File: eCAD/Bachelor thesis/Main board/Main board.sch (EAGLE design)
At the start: 114 parts, among them IC1 ESP32-WROOM-32E_M113EH3200PH3Q, IC10 SMS3.3.TCT, IC2 BC660K-GL, IC3 SMS3.3.TCT, IC4 AP9101CK6-ADTRG1, IC5 FDS6898A, IC6 MCP73871-2CCI_ML, IC7 ME6211C33M5G-N, IC8 ME6211C33M5G-N, IC9 SMS3.3.TCT, J1 U.FL-R-SMT(10), J2 SIM7100-6-1-15-00-A, J3 XT30PW-M, J4 RJE01-660-01, J5 RJE01-660-01, J6 RJE01-660-01, Q1 PDTC114EU,115, Q2 PDTC114EU,115, Q3 IRF7319TRPBF, Q4 IRF7319TRPBF

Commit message: Main board .brd added
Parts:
- removed R35, R36: 10k, rcl:R-EU_R0805
- removed S1, S2, S3, S4, S5: TS-1088-AR02016, 1-component-search:TS-1088-AR02016
- removed TP1, TP2: TPB2,54, testpad:TPB2,54
- added C29: 100n, rcl:C-EUC0805
- added JP10: FAN, jumper:JP2E
- added JP11: LED_VDD, jumper:JP1E
- added JP6: ESP_UART, jumper:JP4E
- added JP8: NB_UART_DEBUG, jumper:JP1E
- added JP9: NTC, jumper:JP1E
- C1: value 470u -> 1u; device rcl:CPOL-EUD -> rcl:C-EUC0805
- C11: value 33p -> 22p
- C13: value 33p -> 100n
- C14: value 100n -> 470u; device rcl:C-EUC0805 -> rcl:CPOL-EUD
- C15: value 100n -> (none)
- C17: value 10u -> 100n
- C18: value 4u7 -> 100n
- C19: value 1u -> 10u
- C2: value 1u -> 470u; device rcl:C-EUC0805 -> rcl:CPOL-EUD
- C20, C23: value 1u -> 4u7
- C21: value 4u7 -> 1u
- C24: value 100n -> 1u
- C25: value 50 -> 1u; device rcl:CPOL-EUE5-10.5 -> rcl:C-EUC0805
- C26: value 22u -> 50; device rcl:C-EUC0805 -> rcl:CPOL-EUE5-10.5
- C4: value 470u -> 22u; device rcl:CPOL-EUD -> rcl:C-EUC0805
- C6: value 22p -> 33p
- C7: value 100p -> 33p
- C9: value (none) -> 100p
- JP1: device pinhead:PINHD-1X3 -> jumper:JP1E
- JP2: value ESP_UART -> (none); device jumper:JP4E -> jumper:JP1E
- JP3: value NB_UART -> (none); device jumper:JP4E -> jumper:JP1E
- JP4: value NTC -> (none)
- JP5: value LED_VDD -> (none)
- JP7: value FAN -> NB_UART; device jumper:JP2E -> jumper:JP4E
- LED1: value STAT1 -> NETSTAT
- R10: value (none) -> 2k7
- R11: value 2k2 -> 1M; device rcl:R-EU_R1206 -> rcl:R-EU_R0805
- R12: value 2k7 -> 5k1
- R13: value 1M -> 5k1
- R14: value 5k1 -> 330R
- R15: value 5k1 -> (none)
- R16: value 330R -> (none)
- R17, R18: value (none) -> 470
- R20, R21: value 470 -> 10k
- R23: value 10k -> 1k
- R24: value 10k -> (none)
- R25: value 1k -> (none)
- R26, R27: value (none) -> 4k7
- R29: value 10k -> 4k7
- R30, R31, R32: value 4k7 -> 10k
- R4: value 10K -> 10k
- R5: value 10K -> 22
- R6: value 10k -> 22
- R8: value 22 -> (none)
- R9: value 22 -> 2k2; device rcl:R-EU_R0805 -> rcl:R-EU_R1206
- renumbered $3_24_$_2023-03-17_12-09-30 to $3_29_$_2023-03-21_17-43-41, $3_25_$_2023-03-17_12-09-30 to $3_30_$_2023-03-21_17-43-41
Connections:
- removed net BAT+: Q3.S2, R33.1
- removed net BOOT_N: IC1.IO19, R4.2, S4.NO
- removed net ESP_PIN: IC1.IO33, Q3.G1, Q4.G1, R28.2, R29.2
- removed net PSM_EINT_N: IC1.IO5, R5.2, S5.NO
- removed net RESET_EN: IC1.IO18, R3.2, S3.NO
- new net DRIVE_PIN: IC1.IO33, Q3.G1, Q4.G1, R28.2, R30.2
- net !PG: now also R17.2, R20.2; no longer R19.2, R22.2
- net !TE1: now also R23.1; no longer R25.1
- net BAT-: now also C18.2; no longer C16.2
- net BAT_Q: now also R20.1, R21.1, R33.2; no longer R23.1, R24.1, R35.2
- net BOOT: now also JP4.1
- net CC3: now also R13.1; no longer R15.1
- net CC4: now also R12.1; no longer R14.1
- net DS18B_SIG: now also R29.1; no longer R32.1
- net ESP_EN: now also C1.1, JP1.2; no longer C2.1, JP1.3, S1.NO
- net ESP_FLASH: now also JP2.2; no longer S2.COM
- net FLASH_RX: now also JP6.3; no longer JP2.3
- net FLASH_TX: now also JP6.2; no longer JP2.2
- net GND: now also C1.2, C14.-, C2.-, C25.2, C26.-, C29.2, C3.2, C4.1, C5.1, JP10.1, JP2.1, JP3.2, JP4.2, JP6.4, JP7.4, JP9.1, R10.1, R11.2, R12.2, R16.2, R23.2, R24.2, R30.1, R34.1; no longer C1.-, C18.2, C2.2, C25.-, C26.1, C3.1, C4.-, C5.2, JP1.2, JP2.4, JP3.4, JP4.1, JP7.1, R12.1, R14.2, R15.2, R18.2, R26.2, R27.2, R29.1, R36.1, R4.1, R5.1, S1.COM, S2.NO
- net G_BAT: now also R31.2; no longer R33.2
- net G_SENS: now also R32.2; no longer R34.2
- net I2C_SCL: now also R27.1; no longer R31.1
- net I2C_SDA: now also R26.1; no longer R30.1
- net N$1: now also JP8.1; no longer TP1.TP
- net N$16: now also R9.2; no longer R11.2
- net N$17: now also R9.1; no longer R11.1
- net N$19: now also C12.1, R8.1; no longer C9.1, R10.1
- net N$2: now also JP8.2; no longer TP2.TP
- net N$20: now also C15.1, R8.2; no longer C12.1, R10.2
- net N$21: now also C7.1, R5.2; no longer C10.1, R7.2
- net N$22: now also C8.1, R6.2; no longer C11.1, R8.2
- net N$23: now also C10.1, R7.2; no longer C13.1, R9.2
- net N$5: now also C18.1, R14.1; no longer C16.1, R16.1
- net N$6: now also IC8.CE, JP10.2; no longer IC7.CE, JP7.2
- net N$7: now also R17.1; no longer R19.1
- net N$8: now also R18.1; no longer R20.1
- net N$9: now also R19.1; no longer R21.1
- net OUT: now also C20.1; no longer C18.1
- net PROG2: now also R24.1; no longer R26.1
- net PROG4: now also R25.1; no longer R27.1
- net PSM_EINT: now also IC1.IO5, JP5.1, R3.2
- net RESET_N: now also C17.1, C3.1, JP3.1; no longer C15.1
- net RESET_QUECTEL: now also IC1.IO18
- net S1: now also R11.1; no longer R13.1
- net SENS_VDD33: now also R26.2, R27.2, R29.2; no longer R30.2, R31.2, R32.2
- net STAT1: now also R19.2, R22.2; no longer R21.2, R24.2
- net STAT2: now also R18.2, R21.2; no longer R20.2, R23.2
- net THERM1: now also JP9.2; no longer JP4.2
- net UART_MCU_RX: now also JP7.2; no longer JP3.2
- net UART_MCU_TX: now also JP7.3; no longer JP3.3
- net USIM_CLK: now also R6.1; no longer R8.1
- net USIM_DATA: now also R4.2, R7.1; no longer R6.2, R9.1
- net USIM_GND: now also C16.2; no longer C14.2
- net USIM_RST: now also R5.1; no longer R7.1
- net USIM_VDD: now also C16.1, C6.1, R4.1; no longer C14.1, C8.1, R6.1
- net VBAT: now also C23.1, Q3.S2, R14.2, R31.1; no longer C21.1, R16.2
- net VDD33: now also C11.1, C13.1, C14.+, C2.+, C24.1, C26.+, C4.2, C5.2, C9.1, IC7.VOUT, JP11.2, JP6.1, JP7.1, R32.1; no longer C1.+, C23.1, C25.+, C26.2, C3.2, C4.+, C5.1, C6.1, C7.1, IC8.VOUT, JP2.1, JP3.1, R34.1, S3.COM, S4.COM, S5.COM
- net VDD_FAN: now also C25.1, IC8.VOUT; no longer C22.1, IC7.VOUT
- net VDD_LED: now also JP11.1; no longer JP5.1
- net VIN: now also C21.1, IC8.VIN, JP10.3, R15.2; no longer C17.1, IC7.VIN, JP7.3, R17.2
- net VIN_LDO: now also C22.1, IC7.CE, IC7.VIN; no longer C20.1, IC8.CE, IC8.VIN
- net VM1: now also R10.2; no longer R12.2
- net VOL_SENS: now also C29.1, R33.1, R34.2; no longer C24.1, R35.1, R36.2
- net VPCC1: now also R15.1, R16.1; no longer R17.1, R18.1
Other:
- moved on the sheet: C10, C11, C12, C13, C15, C18, C19, C20, C21, C22, C23, C3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

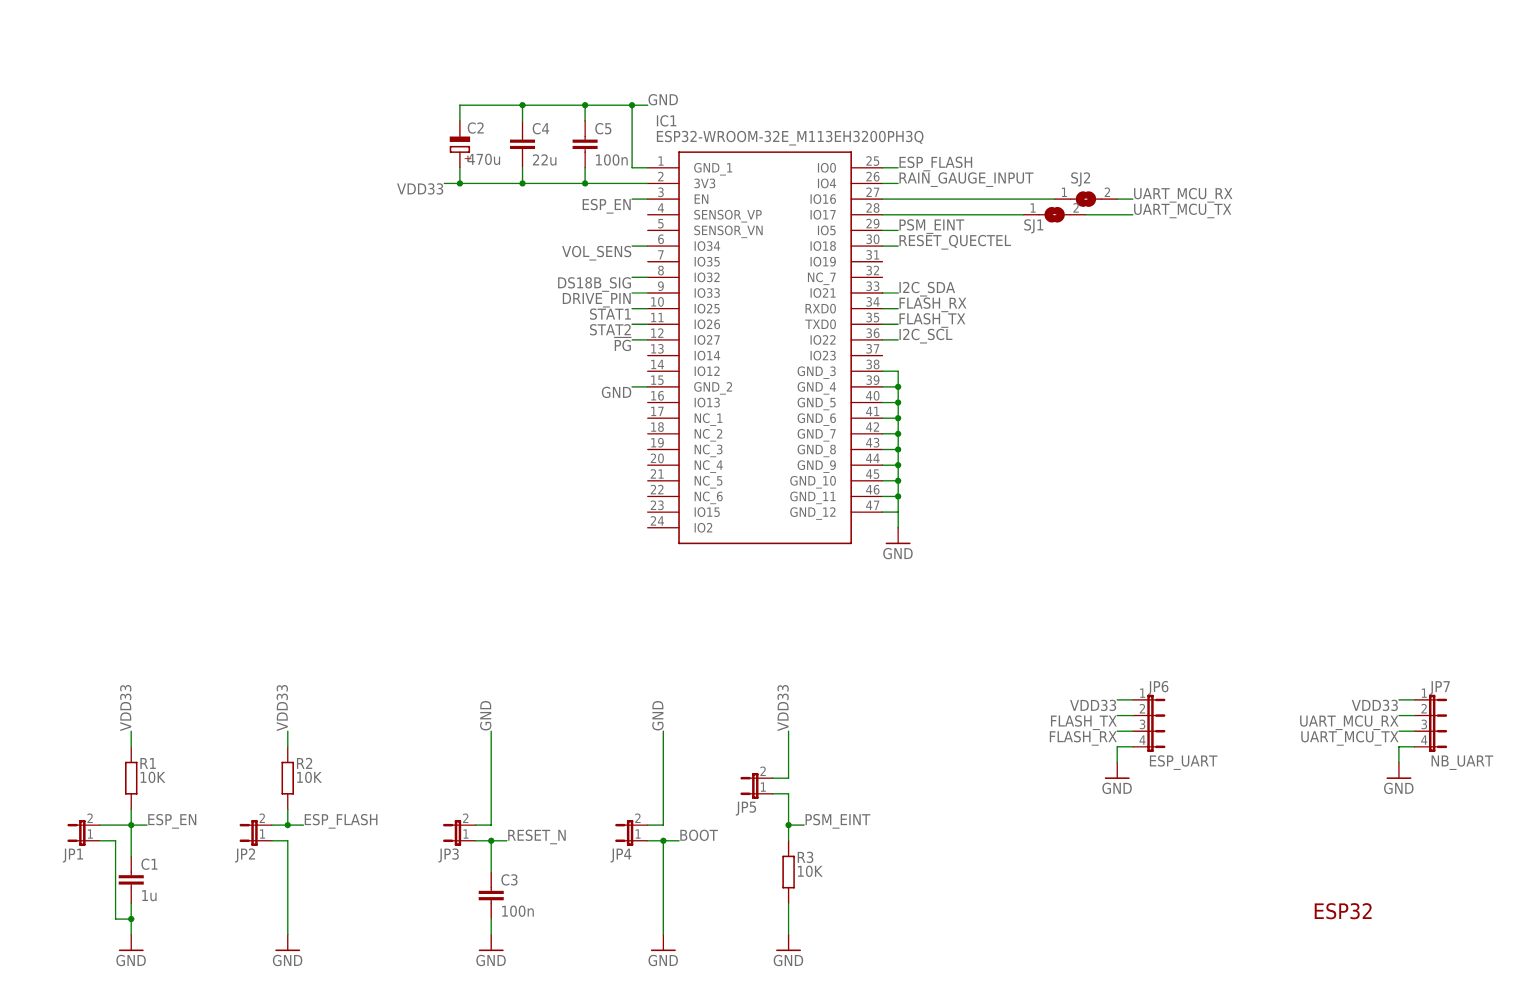
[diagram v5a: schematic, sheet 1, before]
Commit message: component placement
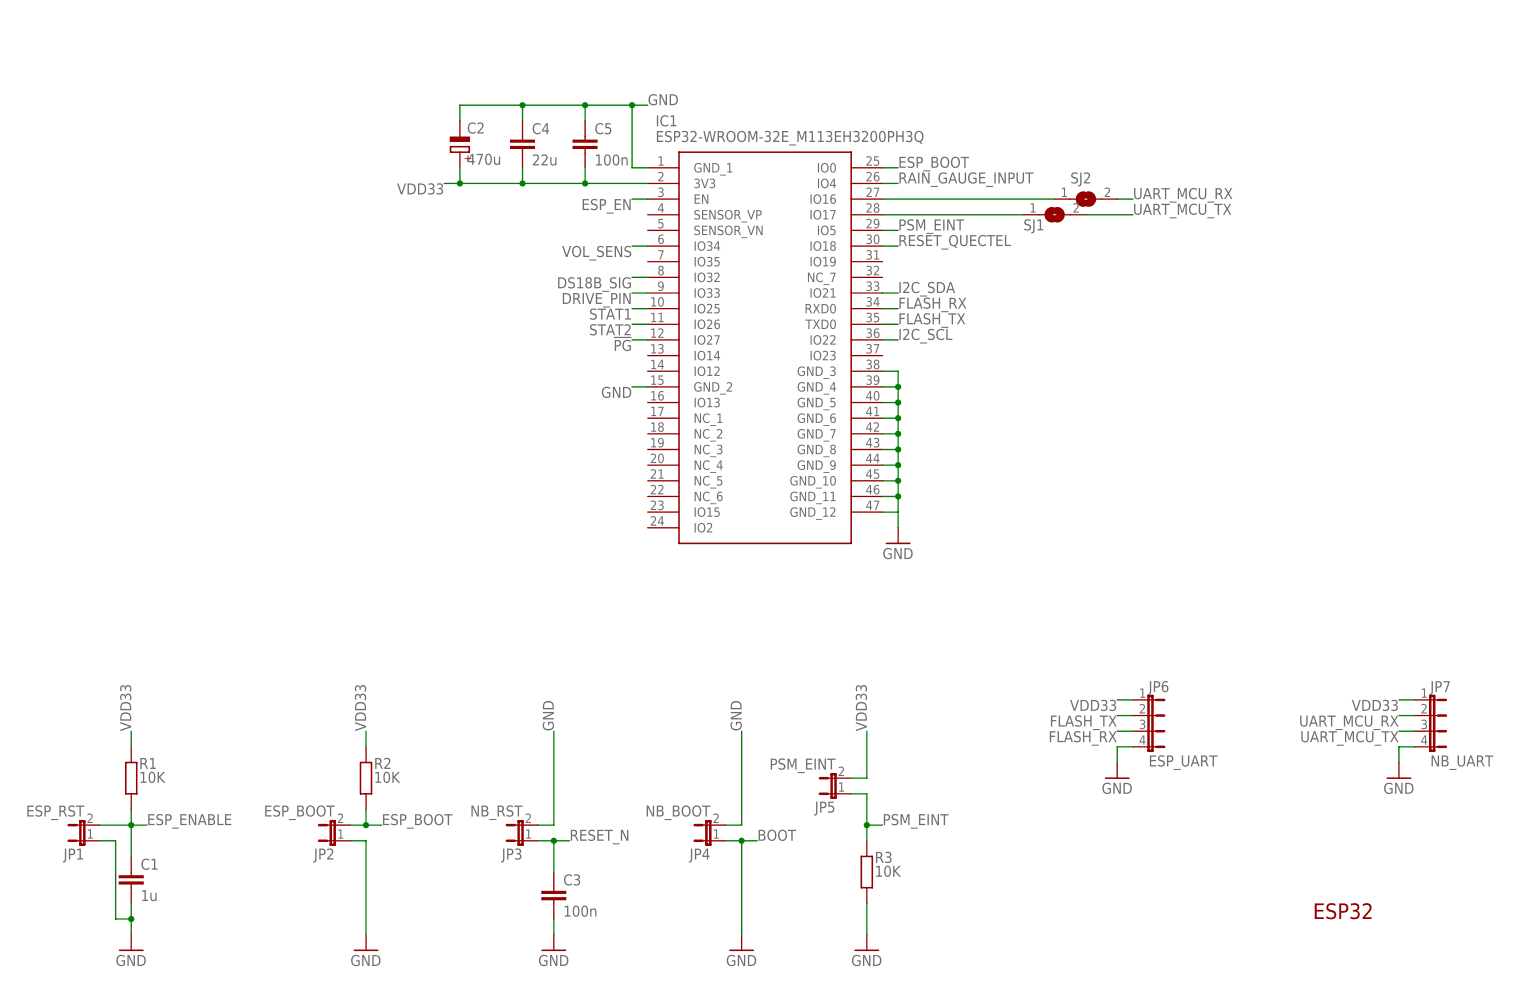
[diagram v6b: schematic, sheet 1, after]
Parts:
- JP1: value (none) -> ESP_RST
- JP2: value (none) -> ESP_BOOT
- JP3: value (none) -> NB_RST
- JP4: value (none) -> NB_BOOT
- JP5: value (none) -> PSM_EINT
- R9: device rcl:R-EU_R1206 -> rcl:R-EU_R0805
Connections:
- net ESP_FLASH renamed ESP_BOOT
- new net ESP_ENABLE: C1.1, JP1.2, R1.1
- net ESP_EN: no longer C1.1, JP1.2, R1.1
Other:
- moved on the sheet: C3, JP2, JP3, JP4, JP5, R2, R3

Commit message: Routing
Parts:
- C1, C10, C11, C12, C13, C15, C16, C17, C18, C19, C20, C21, C22, C23, C24, C25, C3, C4, C5, C6, C7, C8, C9: device rcl:C-EUC0805 -> rcl:C-EUC0603
- D1, D2, D5: value SMBJ6.5A -> PTVS6V5S1UR,115; device 1-component-search:SMBJ6.5A -> 1-component-search:PTVS6V5S1UR,115
- JP10: device jumper:JP2E -> jumper:JP1E
- R1, R11, R12, R13, R14, R17, R18, R19, R2, R20, R21, R22, R23, R3, R4, R5, R6, R7, R8, R9: device rcl:R-EU_R0805 -> rcl:R-EU_R0603
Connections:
- removed net ESP_EN: IC1.EN
- removed net VCC: IC6.PROG2
- net ESP_ENABLE: now also IC1.EN
- net GND: no longer JP10.1
- net N$6: now also JP10.1; no longer JP10.2
- net VIN: now also IC6.PROG2, JP10.2; no longer JP10.3

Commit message: v2 board out in production
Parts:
- C26: value 50 -> 30F
- R1, R2, R3: value 10K -> 10k
- R15: value (none) -> 100k
- R16: value (none) -> 330k
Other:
- note added: "VPCC: 1.23=(R15/R15+R16)*VPCC With 100k and 330k R we get VPCC voltage 5.29 V. For more info see MCP73871 datasheet, chapter 3.3."
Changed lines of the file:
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@@
 </modules>
 <parts>
-<part name="R1" library="rcl" library_urn="urn:adsk.eagle:library:334" deviceset="R-EU_" device="R0603" package3d_urn="urn:adsk.eagle:package:23555/3" value="10K"/>
-<part name="R2" library="rcl" library_urn="urn:adsk.eagle:library:334" deviceset="R-EU_" device="R0603" package3d_urn="urn:adsk.eagle:package:23555/3" value="10K"/>
+<part name="R1" library="rcl" library_urn="urn:adsk.eagle:library:334" deviceset="R-EU_" device="R0603" package3d_urn="urn:adsk.eagle:package:23555/3" value="10k"/>
+<part name="R2" library="rcl" library_urn="urn:adsk.eagle:library:334" deviceset="R-EU_" device="R0603" package3d_urn="urn:adsk.eagle:package:23555/3" value="10k"/>
 <part name="GND3" library="supply1" library_urn="urn:adsk.eagle:library:371" deviceset="GND" device=""/>
 <part name="GND4" library="supply1" library_urn="urn:adsk.eagle:library:371" deviceset="GND" device=""/>
@@
 <part name="GND35" library="supply1" library_urn="urn:adsk.eagle:library:371" deviceset="GND" device=""/>
 <part name="IC8" library="1-component-search" deviceset="ME6211C33M5G-N" device="" override_package3d_urn="urn:adsk.eagle:package:38373060/2" override_package_urn="urn:adsk.eagle:footprint:38373061/1"/>
-<part name="R3" library="rcl" library_urn="urn:adsk.eagle:library:334" deviceset="R-EU_" device="R0603" package3d_urn="urn:adsk.eagle:package:23555/3" value="10K"/>
+<part name="R3" library="rcl" library_urn="urn:adsk.eagle:library:334" deviceset="R-EU_" device="R0603" package3d_urn="urn:adsk.eagle:package:23555/3" value="10k"/>
 <part name="GND38" library="supply1" library_urn="urn:adsk.eagle:library:371" deviceset="GND" device=""/>
 <part name="C2" library="rcl" library_urn="urn:adsk.eagle:library:334" deviceset="CPOL-EU" device="D" package3d_urn="urn:adsk.eagle:package:23424/2" value="470u"/>
@@
 <part name="R11" library="rcl" library_urn="urn:adsk.eagle:library:334" deviceset="R-EU_" device="R0603" package3d_urn="urn:adsk.eagle:package:23555/3" value="1M"/>
 <part name="J3" library="1-component-search" deviceset="XT30PW-M" device=""/>
-<part name="D3" library="1-component-search" deviceset="PMEG2010EJ,115" device=""/>
+<part name="D3" library="1-component-search" deviceset="PMEG2010EJ,115" device="" override_package3d_urn="urn:adsk.eagle:package:39832746/2" override_package_urn="urn:adsk.eagle:footprint:39832747/1"/>
 <part name="SJ3" library="jumper" library_urn="urn:adsk.eagle:library:252" deviceset="SJ" device="" package3d_urn="urn:adsk.eagle:package:15471/1"/>
 <part name="GND27" library="supply1" library_urn="urn:adsk.eagle:library:371" deviceset="GND" device=""/>
@@
 <part name="GND71" library="supply1" library_urn="urn:adsk.eagle:library:371" deviceset="GND" device=""/>
 <part name="GND72" library="supply1" library_urn="urn:adsk.eagle:library:371" deviceset="GND" device=""/>
-<part name="R15" library="rcl" library_urn="urn:adsk.eagle:library:334" deviceset="R-EU_" device="R0805" package3d_urn="urn:adsk.eagle:package:23553/2"/>
-<part name="R16" library="rcl" library_urn="urn:adsk.eagle:library:334" deviceset="R-EU_" device="R0805" package3d_urn="urn:adsk.eagle:package:23553/2"/>
+<part name="R15" library="rcl" library_urn="urn:adsk.eagle:library:334" deviceset="R-EU_" device="R0805" package3d_urn="urn:adsk.eagle:package:23553/2" value="100k"/>
+<part name="R16" library="rcl" library_urn="urn:adsk.eagle:library:334" deviceset="R-EU_" device="R0805" package3d_urn="urn:adsk.eagle:package:23553/2" value="330k"/>
 <part name="R25" library="rcl" library_urn="urn:adsk.eagle:library:334" deviceset="R-EU_" device="R0805" package3d_urn="urn:adsk.eagle:package:23553/2"/>
 <part name="R20" library="rcl" library_urn="urn:adsk.eagle:library:334" deviceset="R-EU_" device="R0603" package3d_urn="urn:adsk.eagle:package:23555/3" value="10k"/>
 <part name="R21" library="rcl" library_urn="urn:adsk.eagle:library:334" deviceset="R-EU_" device="R0603" package3d_urn="urn:adsk.eagle:package:23555/3" value="10k"/>
 <part name="R22" library="rcl" library_urn="urn:adsk.eagle:library:334" deviceset="R-EU_" device="R0603" package3d_urn="urn:adsk.eagle:package:23555/3" value="10k"/>
-<part name="C26" library="rcl" library_urn="urn:adsk.eagle:library:334" deviceset="CPOL-EU" device="E5-10.5" package3d_urn="urn:adsk.eagle:package:23372/2" value="50"/>
+<part name="C26" library="rcl" library_urn="urn:adsk.eagle:library:334" deviceset="CPOL-EU" device="E5-10.5" package3d_urn="urn:adsk.eagle:package:23372/2" value="30F"/>
 <part name="GND14" library="supply1" library_urn="urn:adsk.eagle:library:371" deviceset="GND" device=""/>
 <part name="C4" library="rcl" library_urn="urn:adsk.eagle:library:334" deviceset="C-EU" device="C0603" package3d_urn="urn:adsk.eagle:package:23616/2" value="22u"/>
@@
 <part name="JP10" library="jumper" library_urn="urn:adsk.eagle:library:252" deviceset="JP1E" device="" package3d_urn="urn:adsk.eagle:package:15455/1" value="FAN"/>
 <part name="D2" library="1-component-search" deviceset="PTVS6V5S1UR,115" device=""/>
-<part name="D1" library="1-component-search" deviceset="PTVS6V5S1UR,115" device=""/>
+<part name="D1" library="1-component-search" deviceset="PTVS6V5S1UR,115" device="" override_package3d_urn="urn:adsk.eagle:package:39832749/2" override_package_urn="urn:adsk.eagle:footprint:39832750/1"/>
 <part name="D5" library="1-component-search" deviceset="PTVS6V5S1UR,115" device=""/>
 </parts>
@@
 <plain>
 <text x="217.17" y="20.32" size="2.032" layer="94">Power</text>
+<text x="165.1" y="154.94" size="1.778" layer="97">VPCC: 1.23=(R15/R15+R16)*VPCC
+With 100k and 330k R we get VPCC voltage 5.29 V.
+For more info see MCP73871 datasheet, chapter 3.3.</text>
+<text x="172.72" y="157.48" size="1.778" layer="97"></text>
 </plain>
 <instances>
@@
 </instance>
 <instance part="R15" gate="G$1" x="124.46" y="152.4" smashed="yes" rot="R90">
-<attribute name="NAME" x="125.73" y="156.4386" size="1.778" layer="95"/>
-<attribute name="VALUE" x="122.682" y="148.59" size="1.778" layer="96" rot="R90"/>
+<attribute name="NAME" x="125.73" y="158.9786" size="1.778" layer="95"/>
+<attribute name="VALUE" x="125.73" y="156.718" size="1.778" layer="96"/>
 </instance>
 <instance part="R16" gate="G$1" x="132.08" y="152.4" smashed="yes" rot="R90">
 <attribute name="NAME" x="133.35" y="156.4386" size="1.778" layer="95"/>
-<attribute name="VALUE" x="130.302" y="148.59" size="1.778" layer="96" rot="R90"/>
+<attribute name="VALUE" x="133.35" y="154.178" size="1.778" layer="96"/>
 </instance>
 <instance part="R25" gate="G$1" x="185.42" y="116.84" smashed="yes" rot="R270">
@@
 <segment>
 <pinref part="IC6" gate="G$1" pin="SEL"/>
-<wire x1="137.16" y1="127" x2="121.92" y2="127" width="0.1524" layer="91"/>
+<wire x1="137.16" y1="127" x2="119.38" y2="127" width="0.1524" layer="91"/>
 <pinref part="IC6" gate="G$1" pin="CE"/>
 <wire x1="157.48" y1="154.94" x2="157.48" y2="165.1" width="0.1524" layer="91"/>
@@
 <pinref part="C19" gate="G$1" pin="1"/>
 <wire x1="152.4" y1="165.1" x2="124.46" y2="165.1" width="0.1524" layer="91"/>
-<wire x1="124.46" y1="165.1" x2="121.92" y2="165.1" width="0.1524" layer="91"/>
-<wire x1="121.92" y1="165.1" x2="111.76" y2="165.1" width="0.1524" layer="91"/>
+<wire x1="124.46" y1="165.1" x2="119.38" y2="165.1" width="0.1524" layer="91"/>
+<wire x1="119.38" y1="165.1" x2="111.76" y2="165.1" width="0.1524" layer="91"/>
 <wire x1="111.76" y1="165.1" x2="104.14" y2="165.1" width="0.1524" layer="91"/>
 <wire x1="111.76" y1="160.02" x2="111.76" y2="165.1" width="0.1524" layer="91"/>
@@
 <wire x1="124.46" y1="157.48" x2="124.46" y2="165.1" width="0.1524" layer="91"/>
 <junction x="124.46" y="165.1"/>
-<wire x1="121.92" y1="127" x2="121.92" y2="165.1" width="0.1524" layer="91"/>
-<junction x="121.92" y="165.1"/>
+<wire x1="119.38" y1="127" x2="119.38" y2="165.1" width="0.1524" layer="91"/>
+<junction x="119.38" y="165.1"/>
 </segment>
 <segment>
@@
 </drawing>
 <compatibility>
+<note version="6.3" minversion="6.2.2" severity="warning">
+Since Version 6.2.2 text objects can contain more than one line,
+which will not be processed correctly with this version.
+</note>
 <note version="8.2" severity="warning">
 Since Version 8.2, EAGLE supports online libraries. The ids
